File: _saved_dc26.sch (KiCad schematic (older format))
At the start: 641 parts, among them U1 STM32F405RGTx

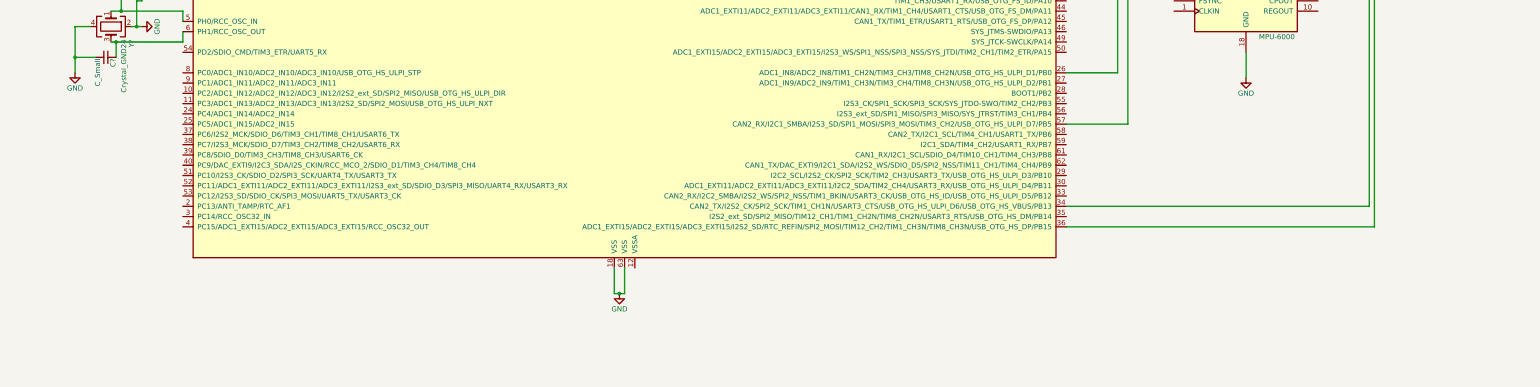
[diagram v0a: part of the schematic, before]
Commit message: Top cutout + mpu6000 + spi connections
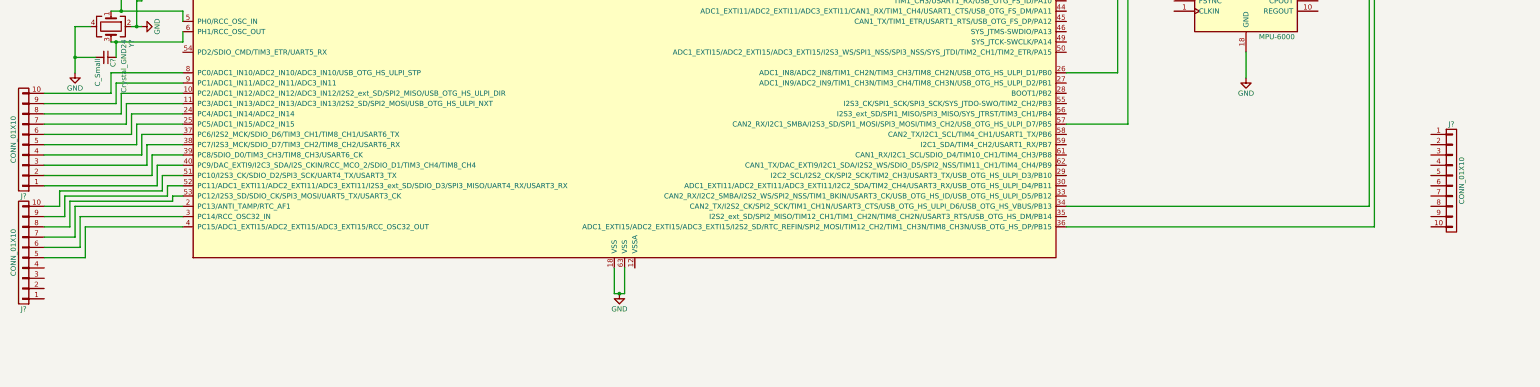
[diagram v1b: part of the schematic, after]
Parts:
- added J? (x3): CONN_01X10, symbol CONN_01X10
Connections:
- net at U1.10 (PC2/ADC1_IN12/ADC2_IN12/ADC3_IN12/I2S2_ext_SD/SPI2_MISO/USB_OTG_HS_ULPI_DIR): now also J?.8 (P8)
- net at U1.11 (PC3/ADC1_IN13/ADC2_IN13/ADC3_IN13/I2S2_SD/SPI2_MOSI/USB_OTG_HS_ULPI_NXT): now also J?.7 (P7)
- net at U1.2 (PC13/ANTI_TAMP/RTC_AF1): now also J?.7 (P7)
- net at U1.24 (PC4/ADC1_IN14/ADC2_IN14): now also J?.6 (P6)
- net at U1.25 (PC5/ADC1_IN15/ADC2_IN15): now also J?.5 (P5)
- net at U1.3 (PC14/RCC_OSC32_IN): now also J?.6 (P6)
- net at U1.37 (PC6/I2S2_MCK/SDIO_D6/TIM3_CH1/TIM8_CH1/USART6_TX): now also J?.4 (P4)
- net at U1.38 (PC7/I2S3_MCK/SDIO_D7/TIM3_CH2/TIM8_CH2/USART6_RX): now also J?.3 (P3)
- net at U1.39 (PC8/SDIO_D0/TIM3_CH3/TIM8_CH3/USART6_CK): now also J?.2 (P2)
- net at U1.4 (PC15/ADC1_EXTI15/ADC2_EXTI15/ADC3_EXTI15/RCC_OSC32_OUT): now also J?.5 (P5)
- net at U1.40 (PC9/DAC_EXTI9/I2C3_SDA/I2S_CKIN/RCC_MCO_2/SDIO_D1/TIM3_CH4/TIM8_CH4): now also J?.1 (P1)
- net at U1.51 (PC10/I2S3_CK/SDIO_D2/SPI3_SCK/UART4_TX/USART3_TX): now also J?.10 (P10)
- net at U1.52 (PC11/ADC1_EXTI11/ADC2_EXTI11/ADC3_EXTI11/I2S3_ext_SD/SDIO_D3/SPI3_MISO/UART4_RX/USART3_RX): now also J?.9 (P9)
- net at U1.53 (PC12/I2S3_SD/SDIO_CK/SPI3_MOSI/UART5_TX/USART3_CK): now also J?.8 (P8)
- net at U1.8 (PC0/ADC1_IN10/ADC2_IN10/ADC3_IN10/USB_OTG_HS_ULPI_STP): now also J?.10 (P10)
- net at U1.9 (PC1/ADC1_IN11/ADC2_IN11/ADC3_IN11): now also J?.9 (P9)
